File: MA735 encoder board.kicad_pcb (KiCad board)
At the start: 2 copper layers, 5.7 x 105.4 mm, 4 parts, among them J1 FPC contacts 0.3mm, U1 MA735GGU-Z

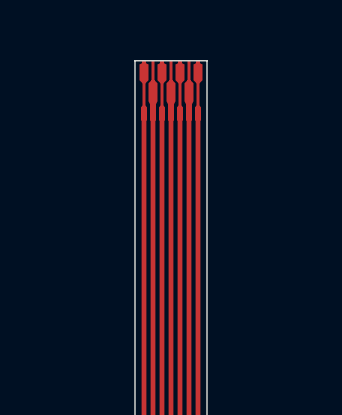
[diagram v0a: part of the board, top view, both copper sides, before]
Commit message: Updated FPC connector to avoid clearance issues and be more consistant
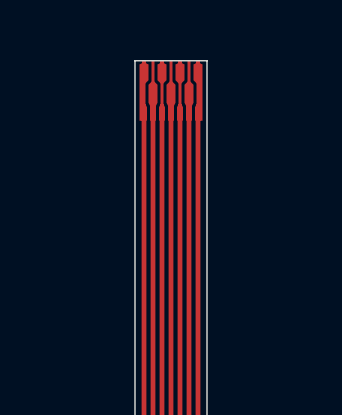
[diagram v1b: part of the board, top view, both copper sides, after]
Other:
- board text added: "Fits connector: Panasonic AYF330735 & Aces 51688-0070M"
- board text removed: "Fits connector: AYF330735 from panasonic"
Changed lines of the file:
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@@
 				(gr_poly
 					(pts
-						(xy -0.1 0.55) (xy -0.05 0.5) (xy 0.05 0.5) (xy 0.1 0.55) (xy 0.1 1) (xy -0.1 1)
+						(xy -0.1 0.55) (xy -0.05 0.45) (xy 0.05 0.45) (xy 0.1 0.55) (xy 0.1 1) (xy -0.1 1)
+					)
+					(width 0)
+					(fill yes)
+				)
+				(gr_poly
+					(pts
+						(xy -0.15 -0.35) (xy -0.15 1) (xy -0.05 1) (xy -0.05 -0.25)
 					)
 					(width 0)
@@
 				(gr_poly
 					(pts
-						(xy -0.15 -0.25) (xy -0.05 -0.35) (xy 0.05 -0.35) (xy 0.15 -0.25) (xy 0.15 0.35) (xy 0.1 0.45)
-						(xy -0.1 0.45) (xy -0.15 0.35)
-					)
-					(width 0)
-					(fill yes)
-				)
-				(gr_poly
-					(pts
 						(xy -0.1 0.45) (xy 0.1 0.45) (xy 0.1 1) (xy -0.1 1)
+					)
+					(width 0)
+					(fill yes)
+				)
+				(gr_poly
+					(pts
+						(xy -0.15 -0.2) (xy -0.05 -0.3) (xy 0.05 -0.3) (xy 0.15 -0.2) (xy 0.15 0.4) (xy 0.1 0.5) (xy -0.1 0.5)
+						(xy -0.15 0.4)
 					)
 					(width 0)
@@
 				(gr_poly
 					(pts
-						(xy -0.1 0.55) (xy -0.05 0.5) (xy 0.05 0.5) (xy 0.1 0.55) (xy 0.1 1) (xy -0.1 1)
-					)
-					(width 0)
-					(fill yes)
-				)
-				(gr_poly
-					(pts
-						(xy -0.15 -0.88) (xy -0.12 -0.89) (xy -0.08 -0.91) (xy -0.06 -0.94) (xy -0.05 -0.97) (xy -0.05 -1)
-						(xy 0.05 -1) (xy 0.05 -0.97) (xy 0.06 -0.94) (xy 0.08 -0.91) (xy 0.12 -0.89) (xy 0.15 -0.88) (xy 0.15 -0.35)
-						(xy 0.05 -0.25) (xy -0.05 -0.25) (xy -0.15 -0.35)
+						(xy -0.15 -0.88) (xy -0.12 -0.89) (xy -0.08 -0.91) (xy -0.06 -0.94) (xy -0.05 -0.97) (xy -0.05 -1)
+						(xy 0.05 -1) (xy 0.05 -0.97) (xy 0.06 -0.94) (xy 0.08 -0.91) (xy 0.12 -0.89) (xy 0.15 -0.88) (xy 0.15 -0.35)
+						(xy 0.05 -0.25) (xy -0.05 -0.25) (xy -0.15 -0.35)
+					)
+					(width 0)
+					(fill yes)
+				)
+				(gr_poly
+					(pts
+						(xy -0.1 0.55) (xy -0.05 0.45) (xy 0.05 0.45) (xy 0.1 0.55) (xy 0.1 1) (xy -0.1 1)
 					)
 					(width 0)
@@
 				(gr_poly
 					(pts
-						(xy -0.15 -0.25) (xy -0.05 -0.35) (xy 0.05 -0.35) (xy 0.15 -0.25) (xy 0.15 0.35) (xy 0.1 0.45)
-						(xy -0.1 0.45) (xy -0.15 0.35)
+						(xy -0.15 -0.2) (xy -0.05 -0.3) (xy 0.05 -0.3) (xy 0.15 -0.2) (xy 0.15 0.4) (xy 0.1 0.5) (xy -0.1 0.5)
+						(xy -0.15 0.4)
 					)
 					(width 0)
@@
 				(gr_poly
 					(pts
-						(xy -0.1 0.55) (xy -0.05 0.5) (xy 0.05 0.5) (xy 0.1 0.55) (xy 0.1 1) (xy -0.1 1)
-					)
-					(width 0)
-					(fill yes)
-				)
-				(gr_poly
-					(pts
-						(xy -0.15 -0.88) (xy -0.12 -0.89) (xy -0.08 -0.91) (xy -0.06 -0.94) (xy -0.05 -0.97) (xy -0.05 -1)
-						(xy 0.05 -1) (xy 0.05 -0.97) (xy 0.06 -0.94) (xy 0.08 -0.91) (xy 0.12 -0.89) (xy 0.15 -0.88) (xy 0.15 -0.35)
-						(xy 0.05 -0.25) (xy -0.05 -0.25) (xy -0.15 -0.35)
+						(xy -0.15 -0.88) (xy -0.12 -0.89) (xy -0.08 -0.91) (xy -0.06 -0.94) (xy -0.05 -0.97) (xy -0.05 -1)
+						(xy 0.05 -1) (xy 0.05 -0.97) (xy 0.06 -0.94) (xy 0.08 -0.91) (xy 0.12 -0.89) (xy 0.15 -0.88) (xy 0.15 -0.35)
+						(xy 0.05 -0.25) (xy -0.05 -0.25) (xy -0.15 -0.35)
+					)
+					(width 0)
+					(fill yes)
+				)
+				(gr_poly
+					(pts
+						(xy -0.1 0.55) (xy -0.05 0.45) (xy 0.05 0.45) (xy 0.1 0.55) (xy 0.1 1) (xy -0.1 1)
 					)
 					(width 0)
@@
 				(gr_poly
 					(pts
-						(xy -0.15 -0.25) (xy -0.05 -0.35) (xy 0.05 -0.35) (xy 0.15 -0.25) (xy 0.15 0.35) (xy 0.1 0.45)
-						(xy -0.1 0.45) (xy -0.15 0.35)
+						(xy -0.15 -0.2) (xy -0.05 -0.3) (xy 0.05 -0.3) (xy 0.15 -0.2) (xy 0.15 0.4) (xy 0.1 0.5) (xy -0.1 0.5)
+						(xy -0.15 0.4)
 					)
 					(width 0)
@@
 				(gr_poly
 					(pts
-						(xy -0.1 0.55) (xy -0.05 0.5) (xy 0.05 0.5) (xy 0.1 0.55) (xy 0.1 1) (xy -0.1 1)
+						(xy -0.1 0.55) (xy -0.05 0.45) (xy 0.05 0.45) (xy 0.1 0.55) (xy 0.1 1) (xy -0.1 1)
+					)
+					(width 0)
+					(fill yes)
+				)
+				(gr_poly
+					(pts
+						(xy 0.15 -0.35) (xy 0.15 1) (xy 0.05 1) (xy 0.05 -0.25)
 					)
 					(width 0)
@@
 		)
 	)
-	(gr_text "Fits connector: AYF330735 from panasonic"
-		(at 146.1 25.9 0)
+	(gr_text "Fits connector: Panasonic AYF330735 & Aces 51688-0070M"
+		(at 141.85 25.49 0)
 		(layer "Cmts.User")
 		(effects

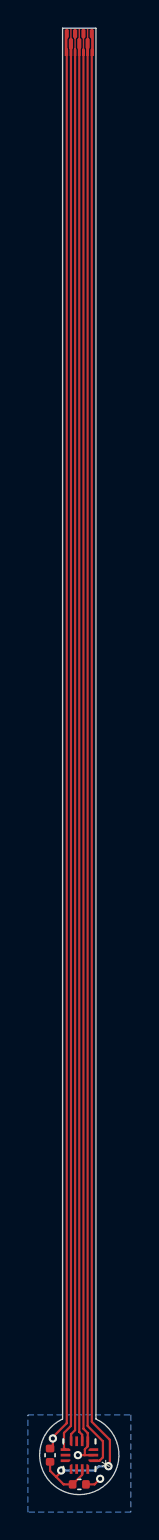
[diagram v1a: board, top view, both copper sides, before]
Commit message: Added Credit on silkscreen
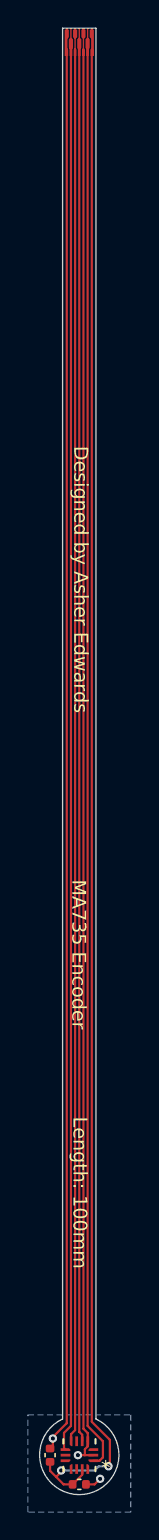
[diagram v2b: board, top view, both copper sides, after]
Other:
- board text added: "Designed by Asher Edwards"
- board text added: "Length: 100mm"
- board text added: "MA735 Encoder"
- board text added: "https://github.com/techy-robot/CACKLE-nanoSPI-MA735_magnetic_encoder"
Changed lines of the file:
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@@
 		(layer "User.2")
+	)
+	(gr_text "Length: 100mm "
+		(at 152.26 107.36 270)
+		(layer "F.SilkS")
+		(effects
+			(font
+				(size 1 1)
+				(thickness 0.1)
+			)
+			(justify left bottom)
+		)
+	)
+	(gr_text "Designed by Asher Edwards"
+		(at 152.32 59.13 270)
+		(layer "F.SilkS")
+		(effects
+			(font
+				(size 1 1)
+				(thickness 0.1)
+			)
+			(justify left bottom)
+		)
+	)
+	(gr_text "MA735 Encoder"
+		(at 152.18 90.31 270)
+		(layer "F.SilkS")
+		(effects
+			(font
+				(size 1 1)
+				(thickness 0.1)
+			)
+			(justify left bottom)
+		)
+	)
+	(gr_text "https://github.com/techy-robot/CACKLE-nanoSPI-MA735_magnetic_encoder"
+		(at 153.23 50.51 90)
+		(layer "B.SilkS")
+		(effects
+			(font
+				(size 1 1)
+				(thickness 0.1)
+			)
+			(justify left bottom mirror)
+		)
 	)
 	(gr_text "0.1mm thick stiffener"
